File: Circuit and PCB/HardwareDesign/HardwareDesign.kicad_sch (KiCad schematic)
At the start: 25 parts, among them SW1 SW_MEC_5G, U1 AMS1117-3.3, U2 ESP32-WROOM-32D, U3 LM2596S-5, U4 LCD-16X2

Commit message: PCB design complete
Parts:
- removed C6: 100n, symbol Device:C
- removed R4: 100, symbol Device:R
- removed RV1: 10k, symbol Device:R_Potentiometer
- removed SW1: SW_MEC_5G, symbol Switch:SW_MEC_5G
- added P1: 282837-2, Terminal Block:TE_282837-2, symbol 282837-2:282837-2
- added SW1: SW_MEC_5E, Button_Switch_THT:SW_PUSH_6mm_H4.3mm, symbol Switch:SW_MEC_5E
- C1, C2, C4, C5: footprint (none) -> Capacitor_SMD:C_0805_2012Metric
- C3: footprint (none) -> Capacitor_SMD:CP_Elec_6.3x5.7
- C6: renamed from C7; footprint (none) -> Capacitor_SMD:C_0805_2012Metric
- C7: renamed from C8; footprint (none) -> Capacitor_SMD:CP_Elec_6.3x5.7
- C8: renamed from C9; footprint (none) -> Capacitor_SMD:C_0805_2012Metric
- H1x2_1: footprint (none) -> Header_1x2:header_1x2
- L1: footprint (none) -> Inductor_SMD:L_10.4x10.4_H4.8
- R1: footprint (none) -> Resistor_SMD:R_0805_2012Metric
- R2, R3: footprint (none) -> Resistor_SMD:R_0603_1608Metric
- R4: renamed from R5; footprint (none) -> Resistor_SMD:R_0603_1608Metric
- RFID1: footprint (none) -> header_1x8:Header_1x8
- RV1: renamed from RV2; footprint (none) -> pot_10k:Potenciometer 10k
- U2: footprint MODULE_ESP32-WROOM-32D -> ESP32:MODULE_ESP32-WROOM-32D
- U4: footprint (none) -> Header_1x16:Header_1x16
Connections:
- net +5V is gone; now on net 5V: R4.1
- net 5v is gone; now on net 5V: C2.1, C7.1, L1.2, RV1.1, U1.3 (VI), U4.2 (VDD)
- net GND: now also P1.2, SW1.2
- net 5V: now reaches U3.4 (FB)
- net at C1.1, R1.2, U2.3 (EN): now also SW1.1
- net +12V renamed VCC
- net VCC: now also P1.1
- net 3.3v renamed 3.3V
- no-connect marks 0 -> 24
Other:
- moved on the sheet: R4

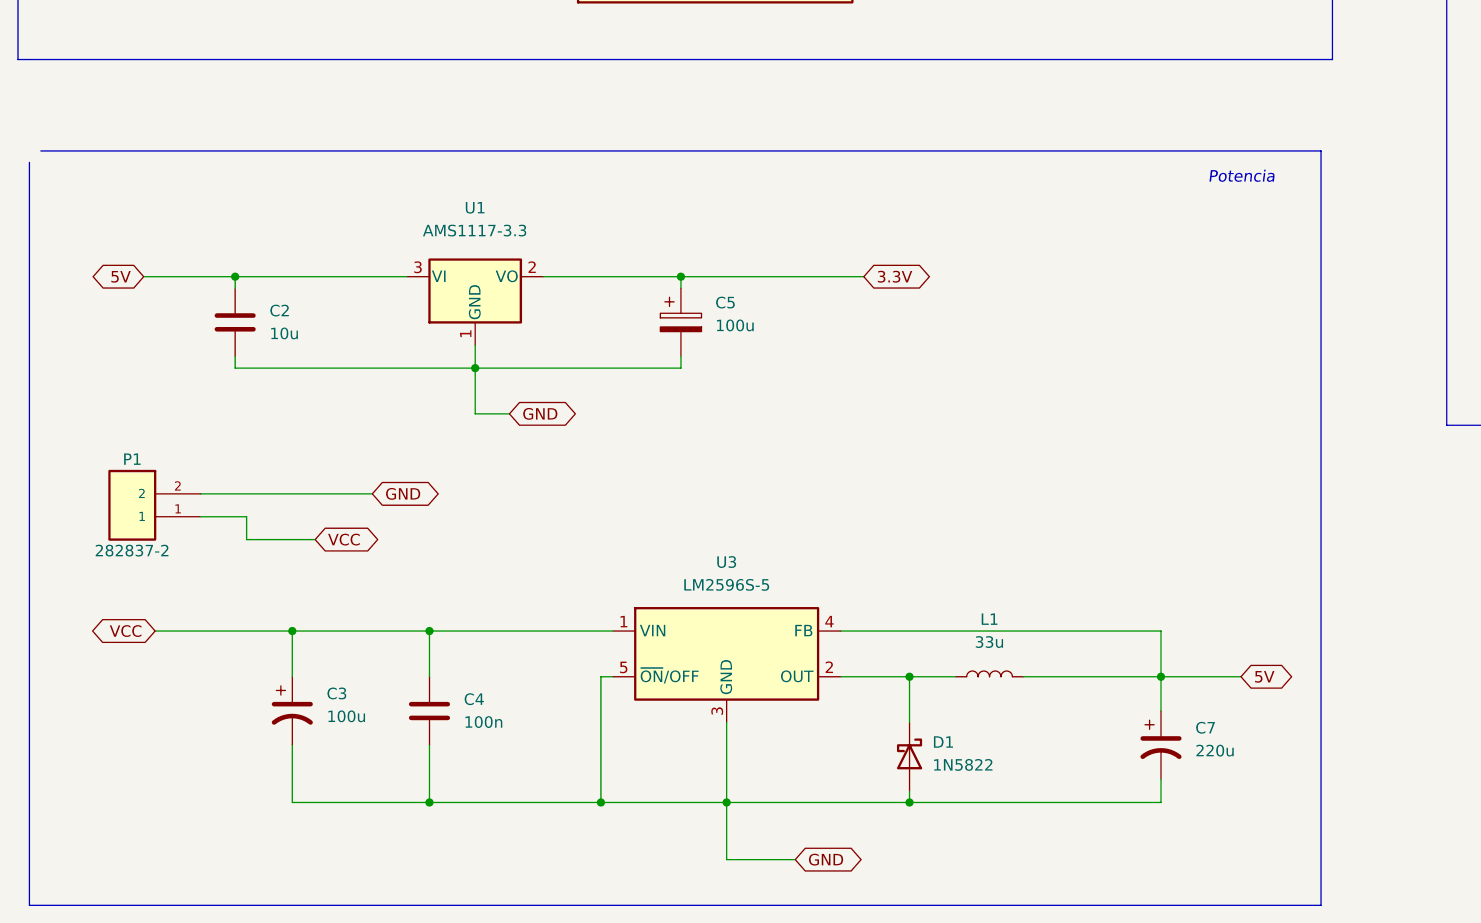
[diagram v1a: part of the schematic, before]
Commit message: add USB-C connector
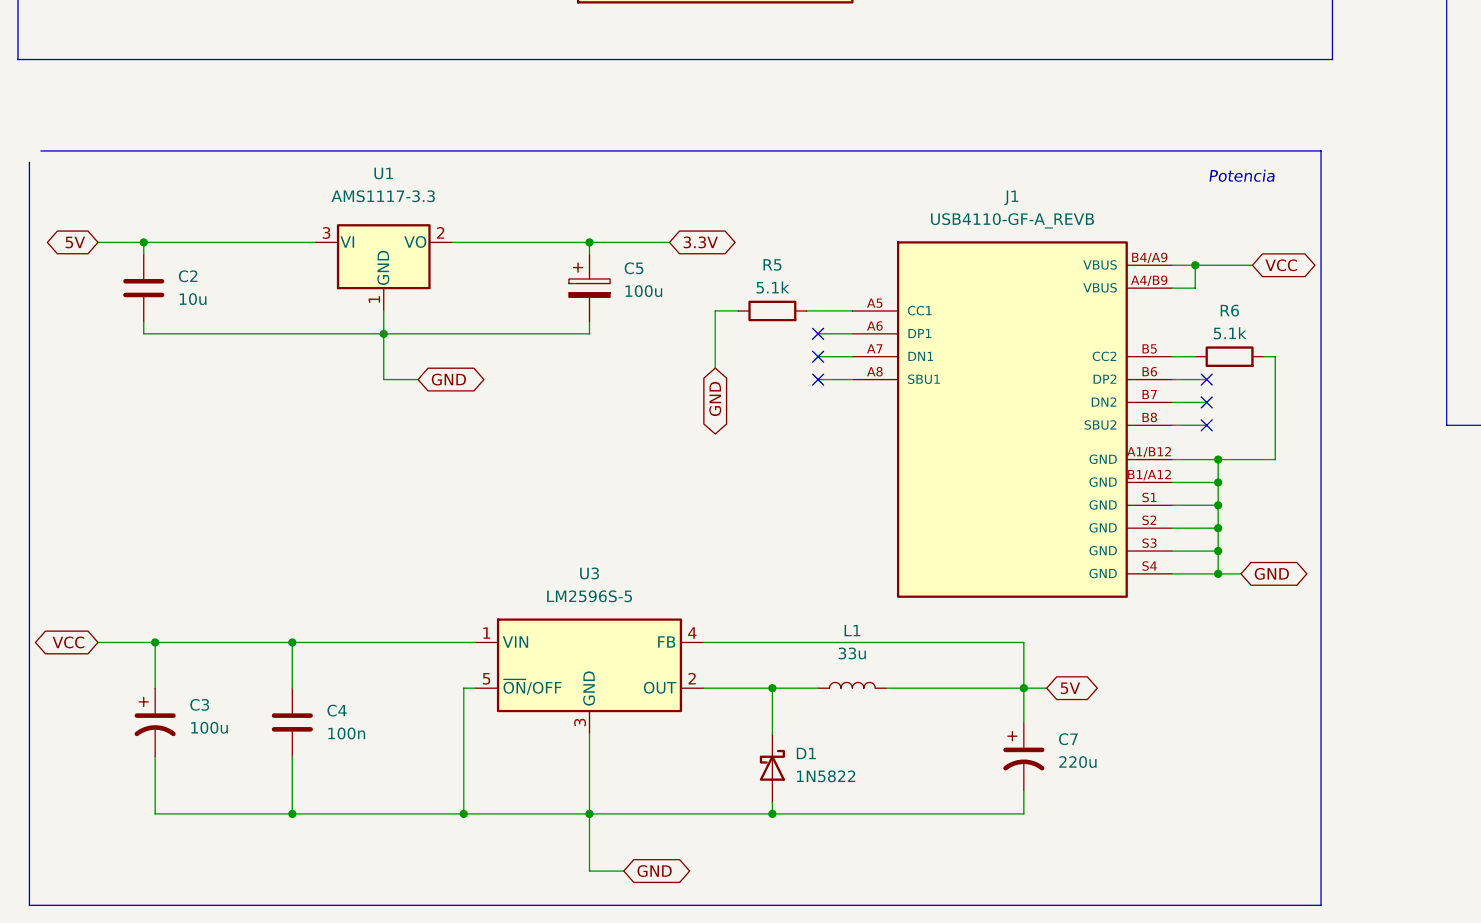
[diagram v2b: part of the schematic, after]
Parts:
- removed P1: 282837-2, Terminal Block:TE_282837-2, symbol 282837-2:282837-2
- added J1: USB4110-GF-A_REVB, USB-C:GCT_USB4110-GF-A_REVB, symbol USB4110-GF-A_REVB:USB4110-GF-A_REVB
- added R5, R6: 5.1k, Resistor_SMD:R_0603_1608Metric, symbol Device:R
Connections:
- net GND: now also J1.A1/B12 (GND), J1.B1/A12 (GND), J1.S1 (GND), J1.S2 (GND), J1.S3 (GND), J1.S4 (GND), R5.1, R6.2
- net VCC: now also J1.A4/B9 (VBUS), J1.B4/A9 (VBUS)
- new net: J1.B5 (CC2), R6.1
- new net: J1.A5 (CC1), R5.2
- no-connect marks 24 -> 30
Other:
- moved on the sheet: C2, C3, C4, C5, C7, D1, L1, U1, U3
